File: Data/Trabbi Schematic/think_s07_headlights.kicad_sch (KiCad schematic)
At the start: 12 parts, among them K1 DRL Relay R5, K2 Park Light Relay R17, SW1 Headlight Switch (C25)

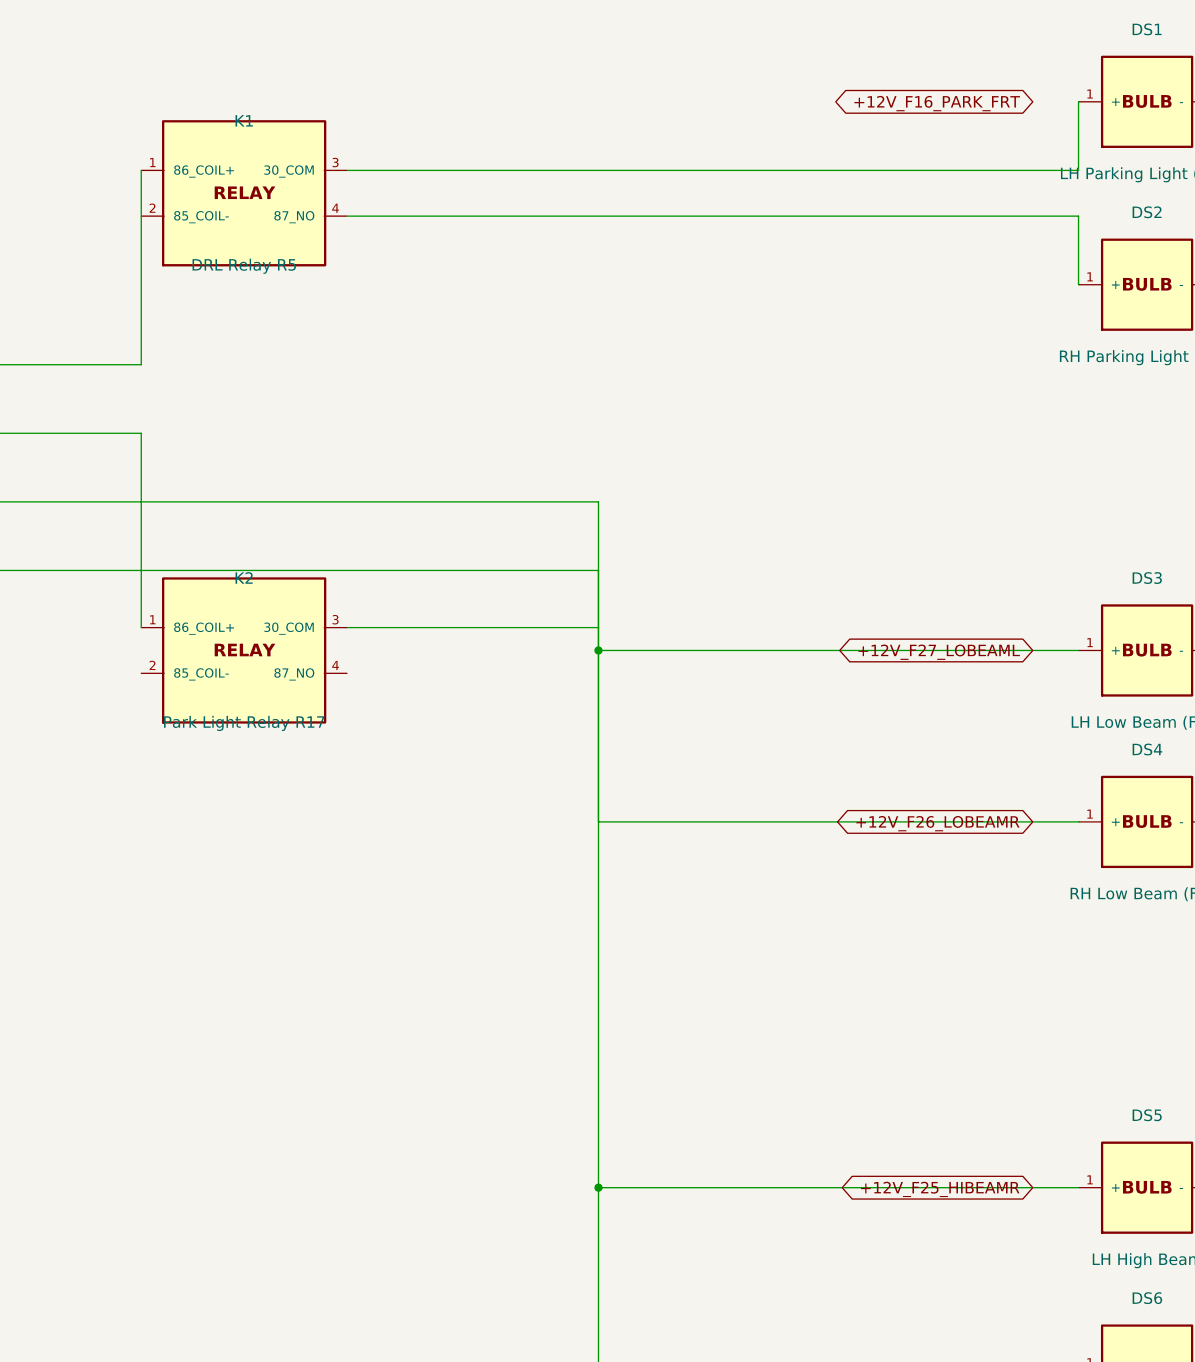
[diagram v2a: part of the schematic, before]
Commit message: Add relay coil/switch graphics, fix label positioning
- Draw coil (inductor arcs) and switch contacts (circles + arm)
  inside RELAY_SPST and RELAY_SPDT symbol bodies
- Add body_gfx parameter to defsym() for custom symbol graphics
- Helper functions: _gfx_polyline, _gfx_arc, _gfx_circle, _relay_gfx
- Fix label offsets: increase from 3-5mm to 10-12mm to avoid
  overlapping pin names (S01 ignition, S02 HV, S05 DCDC, S07 lights)
- Fix S09 turn signal rear labels: add wire stubs (were at 0 offset)
- All 14 schematics regenerated, parentheses balanced, grid OK

Co-Authored-By: Claude Opus 4.6 <noreply@anthropic.com>
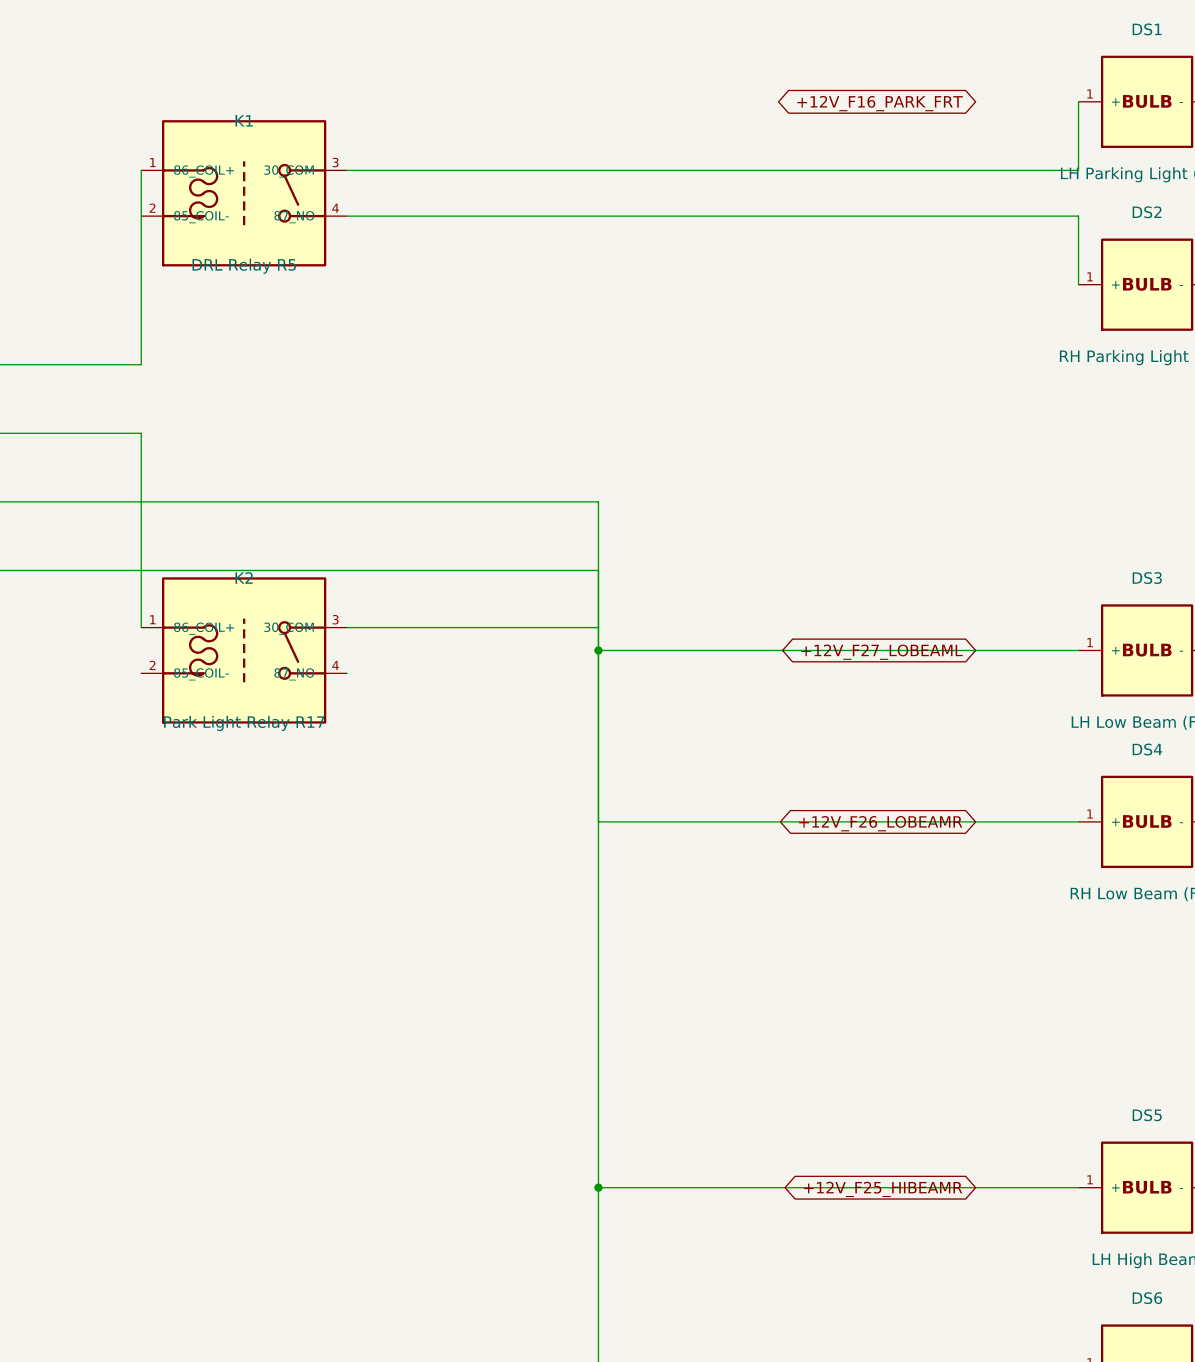
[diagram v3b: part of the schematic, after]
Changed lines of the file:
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@@
     )
   )
-  (global_label "+12V_F16_PARK_FRT" (shape bidirectional) (at 247.650 39.370 180)
+  (global_label "+12V_F16_PARK_FRT" (shape bidirectional) (at 241.300 39.370 180)
     (effects (font (size 1.27 1.27)))
-    (property "Intersheetrefs" "${INTERSHEET_REFS}" (at 247.650 39.370 0)
+    (property "Intersheetrefs" "${INTERSHEET_REFS}" (at 241.300 39.370 0)
       (effects (font (size 1.27 1.27)) hide)
     )
   )
-  (global_label "+12V_F27_LOBEAML" (shape bidirectional) (at 247.650 100.330 180)
+  (global_label "+12V_F27_LOBEAML" (shape bidirectional) (at 241.300 100.330 180)
     (effects (font (size 1.27 1.27)))
-    (property "Intersheetrefs" "${INTERSHEET_REFS}" (at 247.650 100.330 0)
+    (property "Intersheetrefs" "${INTERSHEET_REFS}" (at 241.300 100.330 0)
       (effects (font (size 1.27 1.27)) hide)
     )
   )
-  (global_label "+12V_F26_LOBEAMR" (shape bidirectional) (at 247.650 119.380 180)
+  (global_label "+12V_F26_LOBEAMR" (shape bidirectional) (at 241.300 119.380 180)
     (effects (font (size 1.27 1.27)))
-    (property "Intersheetrefs" "${INTERSHEET_REFS}" (at 247.650 119.380 0)
+    (property "Intersheetrefs" "${INTERSHEET_REFS}" (at 241.300 119.380 0)
       (effects (font (size 1.27 1.27)) hide)
     )
   )
-  (global_label "+12V_F25_HIBEAMR" (shape bidirectional) (at 247.650 160.020 180)
+  (global_label "+12V_F25_HIBEAMR" (shape bidirectional) (at 241.300 160.020 180)
     (effects (font (size 1.27 1.27)))
-    (property "Intersheetrefs" "${INTERSHEET_REFS}" (at 247.650 160.020 0)
+    (property "Intersheetrefs" "${INTERSHEET_REFS}" (at 241.300 160.020 0)
       (effects (font (size 1.27 1.27)) hide)
     )

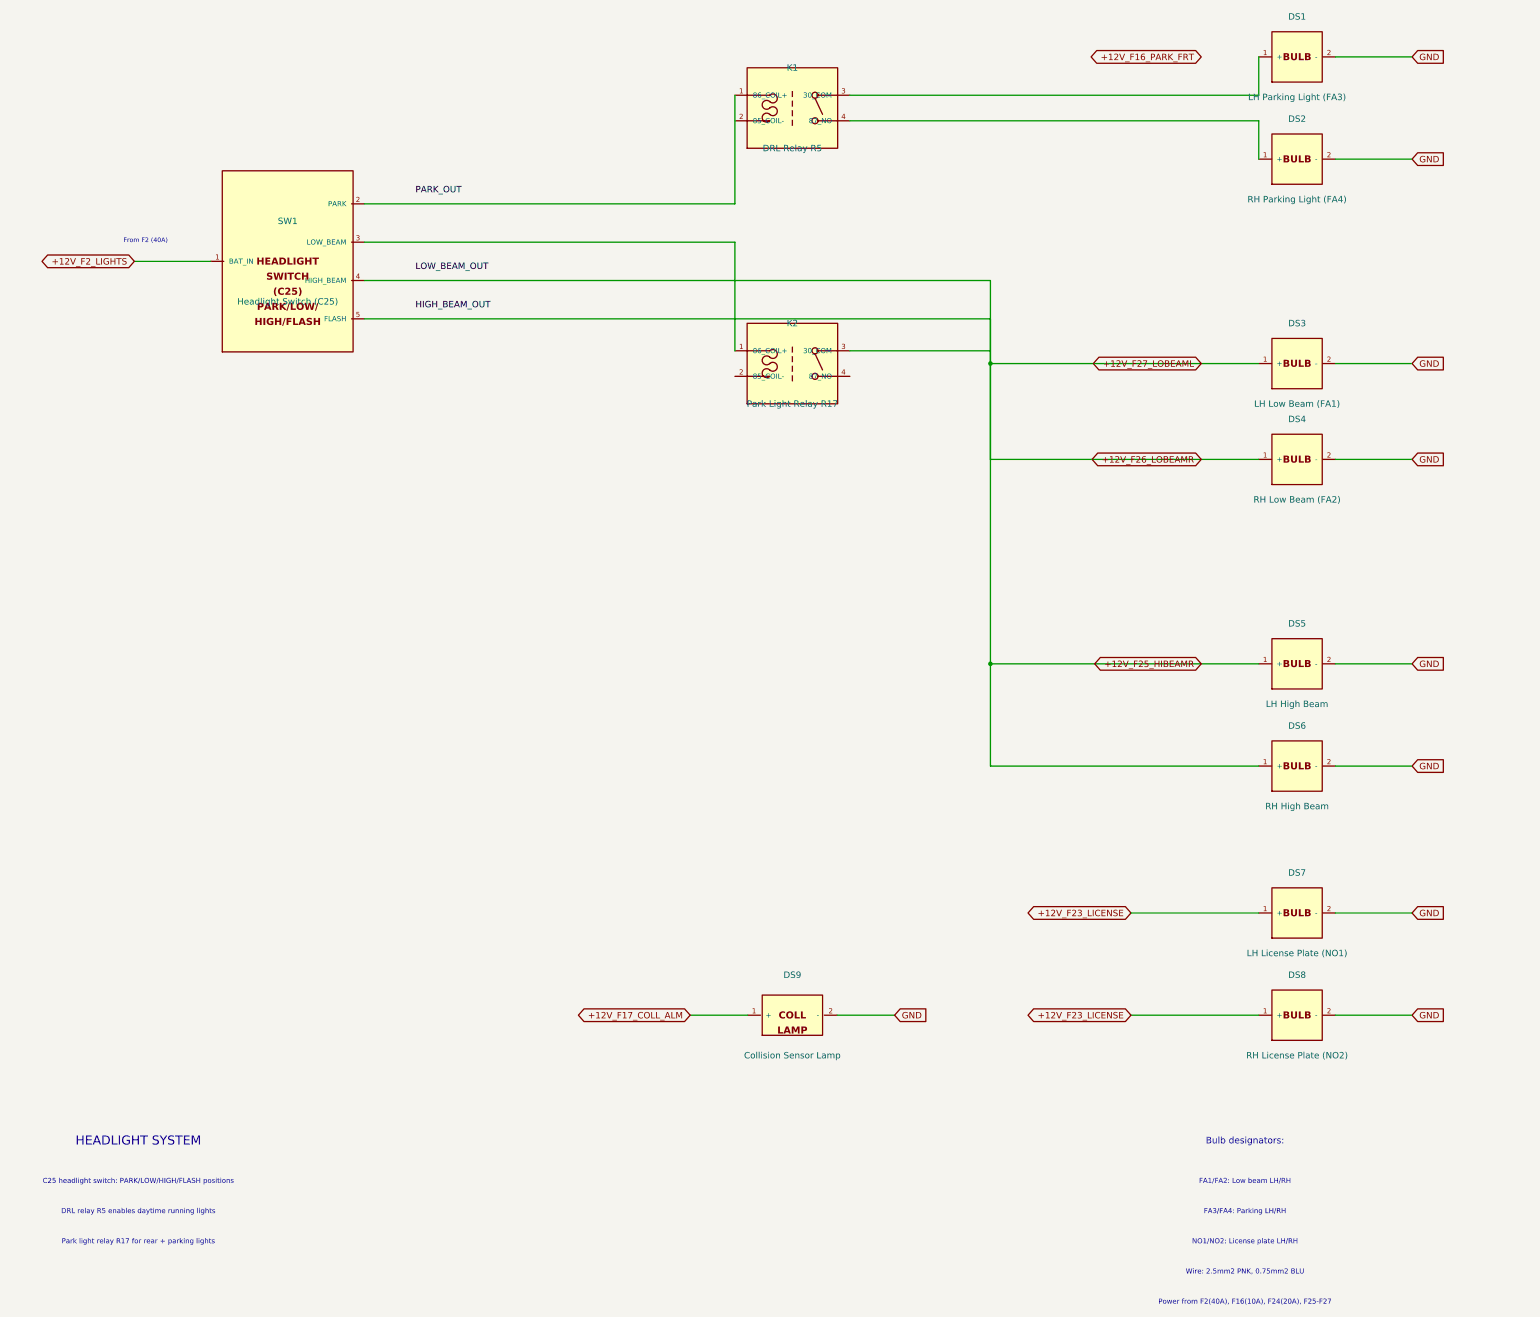
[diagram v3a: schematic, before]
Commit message: Fix label/text positioning: Ref/Value outside body, hide pin numbers
- Reference placed above body edge, Value below (dynamic based on
  symbol height) — no longer overlapping body text
- Pin numbers hidden (clutter, not useful in schematic view)
- Pin name font reduced from 1.016mm to 0.762mm (less overlap)
- Pin length increased from 2.54mm to 3.81mm (more room for pin names
  between body edge and endpoint)
- Store symbol dimensions in _sym_dims for dynamic property placement

Co-Authored-By: Claude Opus 4.6 <noreply@anthropic.com>
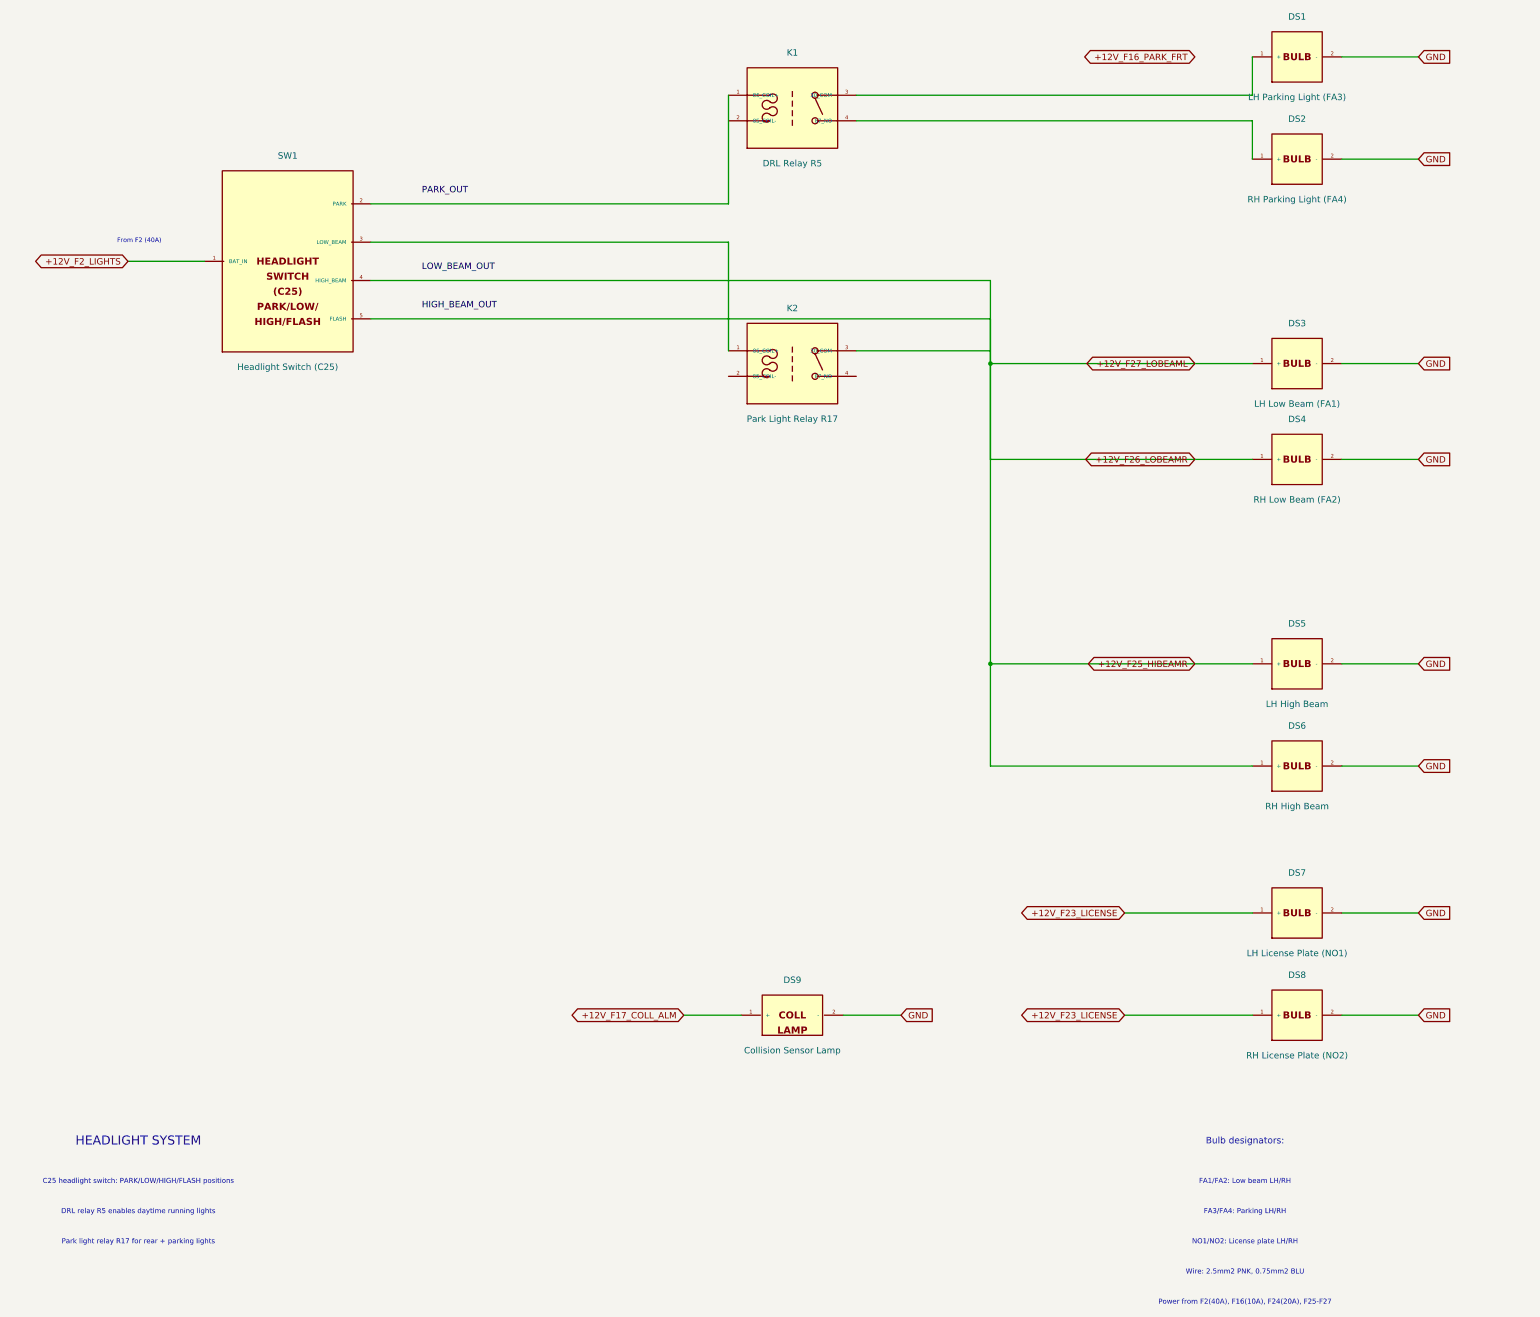
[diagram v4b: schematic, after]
